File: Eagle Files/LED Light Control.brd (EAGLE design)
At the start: 52.5 x 88.1 mm, 18 parts, among them IC2 LM1117DT-3.3, X3 TERMINAL-BLOCK-3.5MM-3-PIN-RO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

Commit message: Tied Ground pin on ESP12E to the GND
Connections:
- net GND: now also U1.GND
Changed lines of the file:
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@@
 <?xml version="1.0" encoding="utf-8"?>
 <!DOCTYPE eagle SYSTEM "eagle.dtd">
-<eagle version="9.1.1">
+<eagle version="9.5.2">
 <drawing>
 <settings>
@@
 </autorouter>
 <elements>
-<element name="C3" library="adafruit" package="C0805" value="1000uF" x="30.988" y="12.192" rot="R90"/>
+<element name="C3" library="adafruit" package="C0805" value="1000uF" x="30.988" y="12.192" smashed="yes" rot="R90">
+<attribute name="NAME" x="29.972" y="11.303" size="1.27" layer="25" rot="R90"/>
+<attribute name="VALUE" x="33.274" y="11.303" size="1.27" layer="27" rot="R90"/>
+</element>
 <element name="CN1" library="adafruit" package="DCJACK_2MM_PTH" value="" x="17.78" y="0" smashed="yes">
 <attribute name="VALUE" x="24.13" y="0" size="1.27" layer="27" rot="R90"/>
 </element>
-<element name="JP1" library="adafruit" package="1X06" value="" x="7.62" y="46.482" rot="R90"/>
-<element name="PGM" library="switch-omron" library_urn="urn:adsk.eagle:library:377" package="B3F-10XX" package3d_urn="urn:adsk.eagle:package:27496/1" value="" x="43.688" y="32.004">
+<element name="JP1" library="adafruit" package="1X06" value="" x="7.62" y="46.482" smashed="yes" rot="R90">
+<attribute name="NAME" x="5.7912" y="38.7858" size="1.27" layer="25" ratio="10" rot="R90"/>
+<attribute name="VALUE" x="10.795" y="38.862" size="1.27" layer="27" rot="R90"/>
+</element>
+<element name="PGM" library="switch-omron" library_urn="urn:adsk.eagle:library:377" package="B3F-10XX" package3d_urn="urn:adsk.eagle:package:27496/1" value="" x="43.688" y="32.004" smashed="yes">
 <attribute name="MF" value="" x="43.688" y="32.004" size="1.778" layer="27" display="off"/>
 <attribute name="MPN" value="B3F-1000" x="43.688" y="32.004" size="1.778" layer="27" display="off"/>
+<attribute name="NAME" x="40.64" y="35.687" size="1.27" layer="25" ratio="10"/>
 <attribute name="OC_FARNELL" value="176432" x="43.688" y="32.004" size="1.778" layer="27" display="off"/>
 <attribute name="OC_NEWARK" value="36M3542" x="43.688" y="32.004" size="1.778" layer="27" display="off"/>
-</element>
-<element name="Q1" library="adafruit" package="SOT23-W" value="" x="36.576" y="17.018" rot="R270"/>
+<attribute name="VALUE" x="40.64" y="26.924" size="1.27" layer="27" ratio="10"/>
+</element>
+<element name="Q1" library="adafruit" package="SOT23-W" value="" x="36.576" y="17.018" smashed="yes" rot="R270">
+<attribute name="NAME" x="36.83" y="14.986" size="0.4064" layer="25" rot="R270"/>
+<attribute name="VALUE" x="36.068" y="14.986" size="0.4064" layer="27" rot="R270"/>
+</element>
 <element name="R10" library="adafruit" package="R0805" value="10K" x="40.64" y="21.082" smashed="yes">
 <attribute name="NAME" x="43.18" y="20.32" size="1.27" layer="25"/>
 <attribute name="VALUE" x="39.878" y="18.796" size="1.27" layer="27"/>
 </element>
-<element name="R3" library="adafruit" package="R0805" value="10kΩ" x="8.128" y="78.486"/>
-<element name="R4" library="adafruit" package="R0805" value="10kΩ" x="8.382" y="74.93"/>
-<element name="R5" library="adafruit" package="R0805" value="10kΩ" x="44.958" y="70.866"/>
-<element name="R6" library="adafruit" package="R0805" value="10kΩ" x="44.958" y="67.056"/>
+<element name="R3" library="adafruit" package="R0805" value="10kΩ" x="8.128" y="78.486" smashed="yes">
+<attribute name="NAME" x="7.366" y="79.502" size="1.27" layer="25"/>
+<attribute name="VALUE" x="7.366" y="76.2" size="1.27" layer="27"/>
+</element>
+<element name="R4" library="adafruit" package="R0805" value="10kΩ" x="8.382" y="74.93" smashed="yes">
+<attribute name="NAME" x="7.62" y="75.946" size="1.27" layer="25"/>
+<attribute name="VALUE" x="7.62" y="72.644" size="1.27" layer="27"/>
+</element>
+<element name="R5" library="adafruit" package="R0805" value="10kΩ" x="44.958" y="70.866" smashed="yes">
+<attribute name="NAME" x="44.196" y="71.882" size="1.27" layer="25"/>
+<attribute name="VALUE" x="44.196" y="68.58" size="1.27" layer="27"/>
+</element>
+<element name="R6" library="adafruit" package="R0805" value="10kΩ" x="44.958" y="67.056" smashed="yes">
+<attribute name="NAME" x="44.196" y="68.072" size="1.27" layer="25"/>
+<attribute name="VALUE" x="44.196" y="64.77" size="1.27" layer="27"/>
+</element>
 <element name="R7" library="adafruit" package="R0805" value="470Ω" x="40.894" y="25.908" smashed="yes" rot="R180">
 <attribute name="NAME" x="45.72" y="26.162" size="1.27" layer="25" rot="R180"/>
 <attribute name="VALUE" x="41.656" y="28.194" size="1.27" layer="27" rot="R180"/>
 </element>
-<element name="R8" library="adafruit" package="R0805" value="300Ω" x="41.656" y="11.938" rot="R270"/>
-<element name="R9" library="adafruit" package="R0805" value="10K" x="30.988" y="17.272" rot="R90"/>
-<element name="U1" library="esp8266modules" package="ESP12E-SMD" value="" x="26.67" y="73.152"/>
+<element name="R8" library="adafruit" package="R0805" value="300Ω" x="41.656" y="11.938" smashed="yes" rot="R270">
+<attribute name="NAME" x="42.672" y="12.7" size="1.27" layer="25" rot="R270"/>
+<attribute name="VALUE" x="39.37" y="12.7" size="1.27" layer="27" rot="R270"/>
+</element>
+<element name="R9" library="adafruit" package="R0805" value="10K" x="30.988" y="17.272" smashed="yes" rot="R90">
+<attribute name="NAME" x="29.972" y="16.51" size="1.27" layer="25" rot="R90"/>
+<attribute name="VALUE" x="33.274" y="16.51" size="1.27" layer="27" rot="R90"/>
+</element>
+<element name="U1" library="esp8266modules" package="ESP12E-SMD" value="" x="26.67" y="73.152" smashed="yes">
+<attribute name="NAME" x="18.97" y="88.252" size="1.4224" layer="25"/>
+<attribute name="VALUE" x="18.97" y="61.252" size="1.4224" layer="27"/>
+</element>
 <element name="X3" library="Rembrandt Electronics - Terminal Block 3-5mm v1-0" package="TERMINAL-BLOCK-3-PIN-3.5MM-ROUND-PAD" value="TERMINAL-BLOCK-3.5MM-3-PIN-ROUND-PAD" x="36.83" y="3.81" smashed="yes">
 <attribute name="VALUE" x="33.0275" y="7.9375" size="1.27" layer="27"/>
 </element>
-<element name="IC2" library="lm1117" package="TO252" value="LM1117DT-3.3" x="16.002" y="29.464">
+<element name="IC2" library="lm1117" package="TO252" value="LM1117DT-3.3" x="16.002" y="29.464" smashed="yes">
 <attribute name="MF" value="Texas Instruments" x="16.002" y="29.464" size="1.778" layer="27" display="off"/>
 <attribute name="MPN" value="LM1117DT-3.3" x="16.002" y="29.464" size="1.778" layer="27" display="off"/>
+<attribute name="NAME" x="12.192" y="26.924" size="1.27" layer="25" rot="R90"/>
 <attribute name="OC_FARNELL" value="1469048" x="16.002" y="29.464" size="1.778" layer="27" display="off"/>
 <attribute name="OC_NEWARK" value="41K3430" x="16.002" y="29.464" size="1.778" layer="27" display="off"/>
-</element>
-<element name="C1" library="adafruit" package="C0805" value="100uF" x="17.526" y="21.082" rot="R180"/>
+<attribute name="VALUE" x="21.082" y="26.924" size="1.27" layer="27" rot="R90"/>
+</element>
+<element name="C1" library="adafruit" package="C0805" value="100uF" x="17.526" y="21.082" smashed="yes" rot="R180">
+<attribute name="NAME" x="18.415" y="20.066" size="1.27" layer="25" rot="R180"/>
+<attribute name="VALUE" x="18.415" y="23.368" size="1.27" layer="27" rot="R180"/>
+</element>
 <element name="C2" library="adafruit" package="C0805" value="100uF" x="15.24" y="37.084" smashed="yes">
 <attribute name="NAME" x="18.161" y="36.576" size="1.27" layer="25"/>
@@
 <contactref element="C1" pad="2"/>
 <contactref element="C2" pad="2"/>
+<contactref element="U1" pad="GND"/>
 </signal>
 <signal name="VCC">

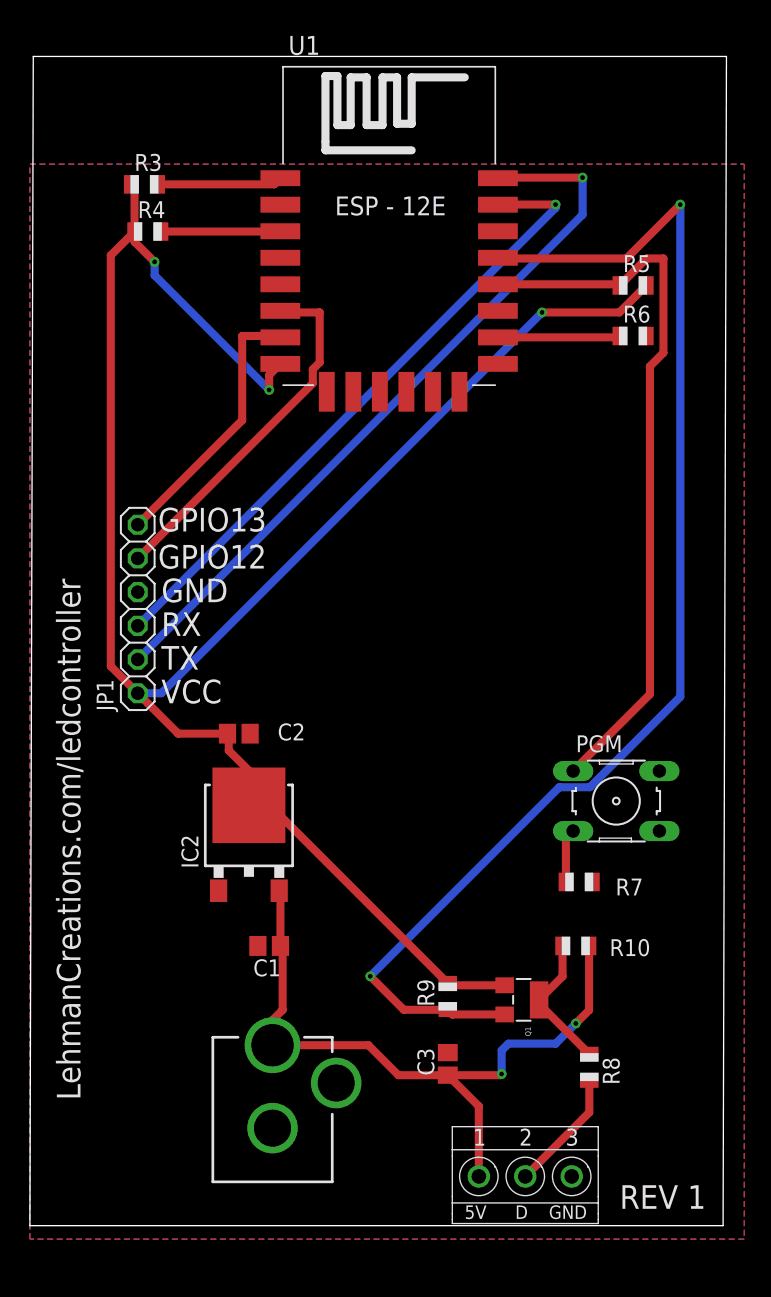
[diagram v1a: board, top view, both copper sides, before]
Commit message: Changed the size of the board to be smaller
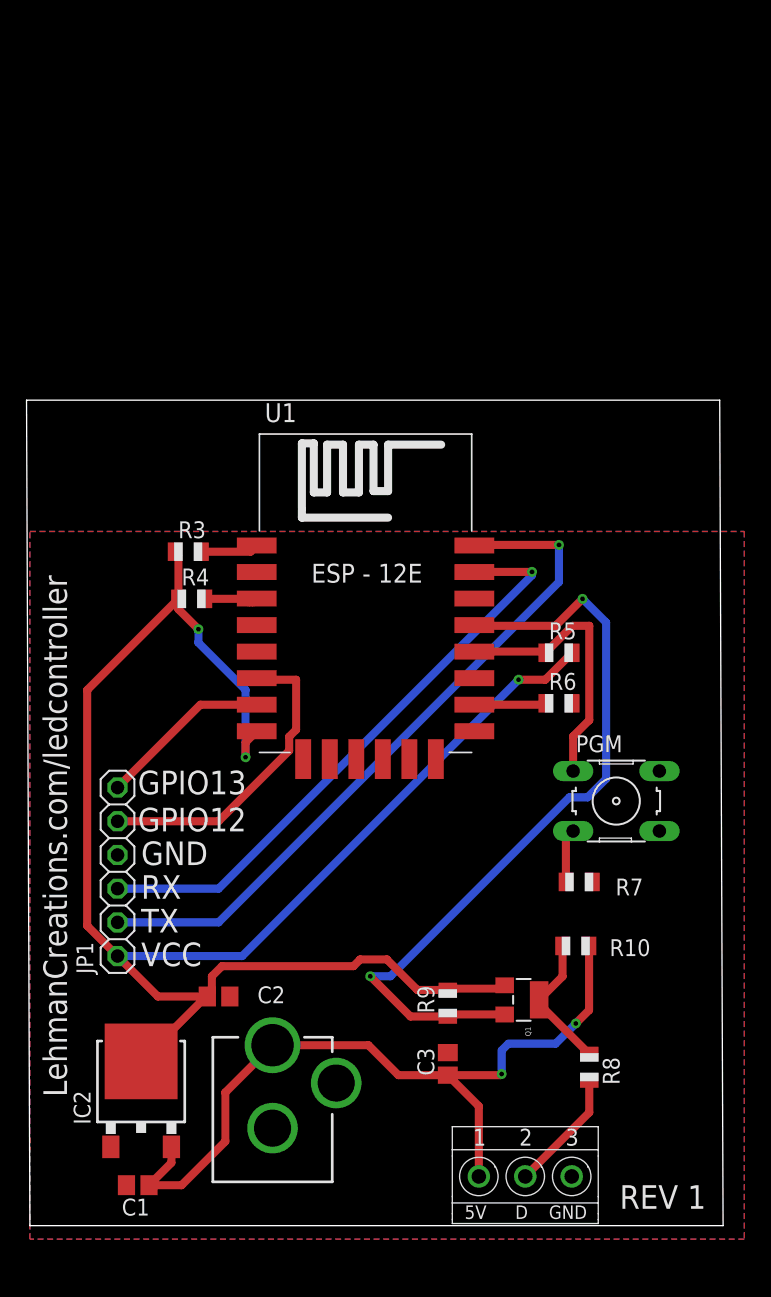
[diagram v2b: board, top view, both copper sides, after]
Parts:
- moved R5 28.2 mm to (39.4, 43.2)
- moved R6 28.2 mm to (39.4, 39.4)
- moved R3 27.9 mm to (11.4, 50.8)
- moved R4 27.9 mm to (11.7, 47.2)
- moved U1 27.7 mm to (24.9, 45.5)
- moved IC2 20.9 mm to (7.87, 10.2)
- moved C1 20.6 mm to (7.62, 3.05)
- moved C2 19.9 mm to (13.7, 17.3)
- moved JP1 19.9 mm to (6.10, 26.7)
- moved R9 0.51 mm to (31.0, 16.8)
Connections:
- net N$9 renamed GPIO0
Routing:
- net DATA: track 96.5 -> 58.7 mm
- net GPIO0: track 54.8 -> 21.0 mm
- net VCC: track 150.0 -> 135.9 mm
- net +5V: track 53.4 -> 60.7 mm
- net GPIO13: track 20.4 -> 13.2 mm
- net N$3: track 9.21 -> 4.13 mm
- net N$2: track 9.44 -> 4.36 mm
- net N$5: track 9.23 -> 5.42 mm
- net TX: track 56.6 -> 53.1 mm
- net RX: track 49.1 -> 45.6 mm
- net GPIO12: track 27.4 -> 23.8 mm
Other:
- board size 52.5 x 88.1 mm -> 52.5 x 62.2 mm
